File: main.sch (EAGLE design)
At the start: 100 parts, among them Q1 5.8A/30V/35mΩ, Q2 5.8A/30V/35mΩ, Q3 2.5A/30V/105mΩ, U2 SN65HVD32_D_8

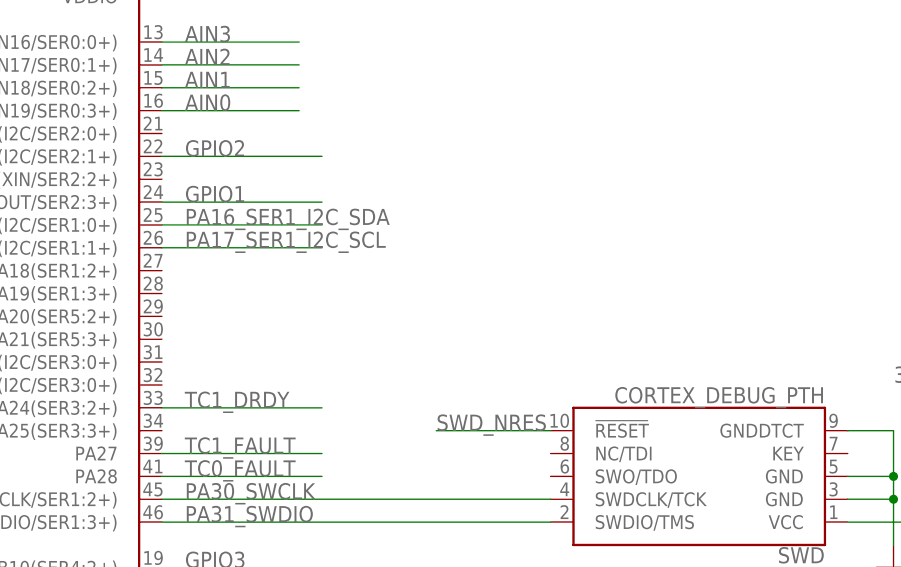
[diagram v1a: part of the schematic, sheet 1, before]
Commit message: Updated 3.3reg values, fixed led resitor, added one led to mcu
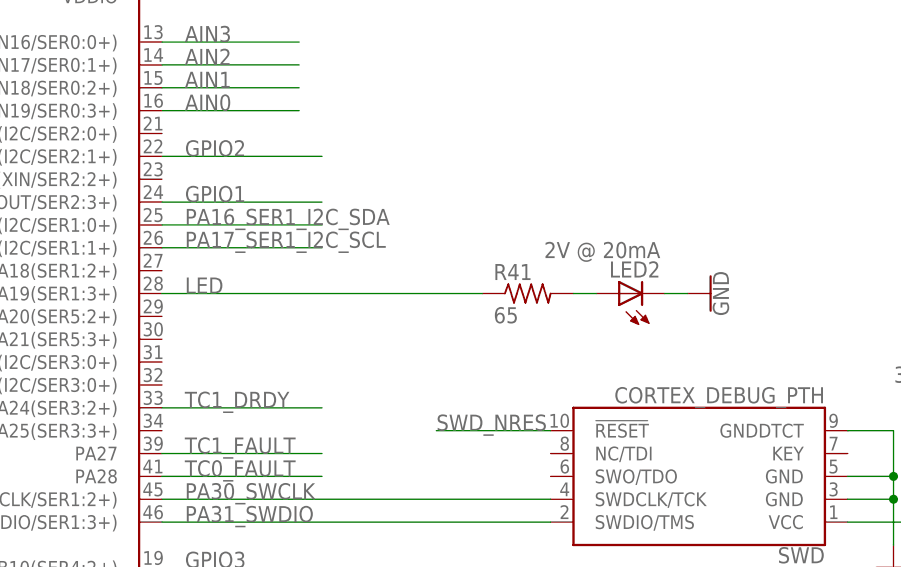
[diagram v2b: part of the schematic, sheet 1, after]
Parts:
- added LED2: 2V @ 20mA, adafruit:LEDCHIPLED_0603
- added R41: 65, resistor:R-US_R0603
- C6: value REF -> 22u
- C7: value REF -> 10u
- L1: value REF -> 2.2u
- LED1: value (none) -> 2V @ 20mA
- R1: value REF -> 470k
- R2: value REF -> 150k
- R3: value REF -> 100k
- R32: value 1.5k -> 65
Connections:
- new net LED: R41.1, SAMD21G18A.PA19(SER1:3+)
- new net N$29: LED2.A, R41.2
- net GND: now also LED2.C
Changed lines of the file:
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@@
 <part name="GND6" library="SparkFun-PowerSymbols" deviceset="GND" device=""/>
 <part name="GND7" library="SparkFun-PowerSymbols" deviceset="GND" device=""/>
-<part name="R1" library="resistor" library_urn="urn:adsk.eagle:library:348" deviceset="R-US_" device="R0603" package3d_urn="urn:adsk.eagle:package:26057/1" value="REF"/>
-<part name="R2" library="resistor" library_urn="urn:adsk.eagle:library:348" deviceset="R-US_" device="R0603" package3d_urn="urn:adsk.eagle:package:26057/1" value="REF"/>
-<part name="R3" library="resistor" library_urn="urn:adsk.eagle:library:348" deviceset="R-US_" device="R0603" package3d_urn="urn:adsk.eagle:package:26057/1" value="REF"/>
-<part name="L1" library="resistor" library_urn="urn:adsk.eagle:library:348" deviceset="L-US" device="L2012C" package3d_urn="urn:adsk.eagle:package:25925/1" value="REF"/>
-<part name="C6" library="resistor" library_urn="urn:adsk.eagle:library:348" deviceset="C-US" device="C0603" package3d_urn="urn:adsk.eagle:package:26138/1" value="REF"/>
+<part name="R1" library="resistor" library_urn="urn:adsk.eagle:library:348" deviceset="R-US_" device="R0603" package3d_urn="urn:adsk.eagle:package:26057/1" value="470k"/>
+<part name="R2" library="resistor" library_urn="urn:adsk.eagle:library:348" deviceset="R-US_" device="R0603" package3d_urn="urn:adsk.eagle:package:26057/1" value="150k"/>
+<part name="R3" library="resistor" library_urn="urn:adsk.eagle:library:348" deviceset="R-US_" device="R0603" package3d_urn="urn:adsk.eagle:package:26057/1" value="100k"/>
+<part name="L1" library="resistor" library_urn="urn:adsk.eagle:library:348" deviceset="L-US" device="L2012C" package3d_urn="urn:adsk.eagle:package:25925/1" value="2.2u"/>
+<part name="C6" library="resistor" library_urn="urn:adsk.eagle:library:348" deviceset="C-US" device="C0603" package3d_urn="urn:adsk.eagle:package:26138/1" value="22u"/>
 <part name="GND8" library="SparkFun-PowerSymbols" deviceset="GND" device=""/>
 <part name="SUPPLY14" library="SparkFun-PowerSymbols" deviceset="3.3V" device=""/>
-<part name="C7" library="rcl" library_urn="urn:adsk.eagle:library:334" deviceset="C-US" device="C1206" package3d_urn="urn:adsk.eagle:package:23618/2" value="REF"/>
+<part name="C7" library="rcl" library_urn="urn:adsk.eagle:library:334" deviceset="C-US" device="C1206" package3d_urn="urn:adsk.eagle:package:23618/2" value="10u"/>
 <part name="POWER_CONTROLLER" library="BQ24133" deviceset="BQ24133_RGY_24" device=""/>
 <part name="SUPPLY3" library="SparkFun-PowerSymbols" deviceset="3.3V" device=""/>
@@
 <part name="R31" library="resistor" library_urn="urn:adsk.eagle:library:348" deviceset="R-US_" device="R0603" package3d_urn="urn:adsk.eagle:package:26057/1" value="30.1k"/>
 <part name="GND36" library="SparkFun-PowerSymbols" deviceset="GND" device=""/>
-<part name="R32" library="resistor" library_urn="urn:adsk.eagle:library:348" deviceset="R-US_" device="R0603" package3d_urn="urn:adsk.eagle:package:26057/1" value="1.5k"/>
-<part name="LED1" library="adafruit" deviceset="LED" device="CHIPLED_0603"/>
+<part name="R32" library="resistor" library_urn="urn:adsk.eagle:library:348" deviceset="R-US_" device="R0603" package3d_urn="urn:adsk.eagle:package:26057/1" value="65"/>
+<part name="LED1" library="adafruit" deviceset="LED" device="CHIPLED_0603" value="2V @ 20mA"/>
 <part name="R_THERM" library="pinhead" library_urn="urn:adsk.eagle:library:325" deviceset="PINHD-1X2" device="" package3d_urn="urn:adsk.eagle:package:22435/2" value="103AT"/>
 <part name="R34" library="resistor" library_urn="urn:adsk.eagle:library:348" deviceset="R-US_" device="R0603" package3d_urn="urn:adsk.eagle:package:26057/1" value="100k"/>
@@
 <part name="R40" library="resistor" library_urn="urn:adsk.eagle:library:348" deviceset="R-US_" device="R0603" package3d_urn="urn:adsk.eagle:package:26057/1" value="10k"/>
 <part name="SUPPLY19" library="SparkFun-PowerSymbols" deviceset="3.3V" device=""/>
+<part name="R41" library="resistor" library_urn="urn:adsk.eagle:library:348" deviceset="R-US_" device="R0603" package3d_urn="urn:adsk.eagle:package:26057/1" value="65"/>
+<part name="LED2" library="adafruit" deviceset="LED" device="CHIPLED_0603" value="2V @ 20mA"/>
+<part name="GND50" library="SparkFun-PowerSymbols" deviceset="GND" device=""/>
 </parts>
 <sheets>
@@
 <instance part="R40" gate="G$1" x="304.8" y="165.1" rot="R90"/>
 <instance part="SUPPLY19" gate="G$1" x="304.8" y="172.72"/>
+<instance part="R41" gate="G$1" x="243.84" y="96.52"/>
+<instance part="LED2" gate="G$1" x="254" y="96.52" rot="R90"/>
+<instance part="GND50" gate="1" x="264.16" y="96.52" rot="R90"/>
 </instances>
 <busses>
@@
 <wire x1="294.64" y1="152.4" x2="304.8" y2="152.4" width="0.1524" layer="91"/>
 </segment>
+<segment>
+<pinref part="GND50" gate="1" pin="GND"/>
+<pinref part="LED2" gate="G$1" pin="C"/>
+<wire x1="261.62" y1="96.52" x2="259.08" y2="96.52" width="0.1524" layer="91"/>
+</segment>
 </net>
 <net name="VDDCORE" class="0">
@@
 </segment>
 </net>
+<net name="LED" class="0">
+<segment>
+<pinref part="R41" gate="G$1" pin="1"/>
+<pinref part="SAMD21G18A" gate="G$1" pin="PA19(SER1:3+)"/>
+<wire x1="238.76" y1="96.52" x2="203.2" y2="96.52" width="0.1524" layer="91"/>
+<label x="205.74" y="96.52" size="1.778" layer="95"/>
+</segment>
+</net>
+<net name="N$29" class="0">
+<segment>
+<pinref part="R41" gate="G$1" pin="2"/>
+<wire x1="248.92" y1="96.52" x2="251.46" y2="96.52" width="0.1524" layer="91"/>
+<pinref part="LED2" gate="G$1" pin="A"/>
+</segment>
+</net>

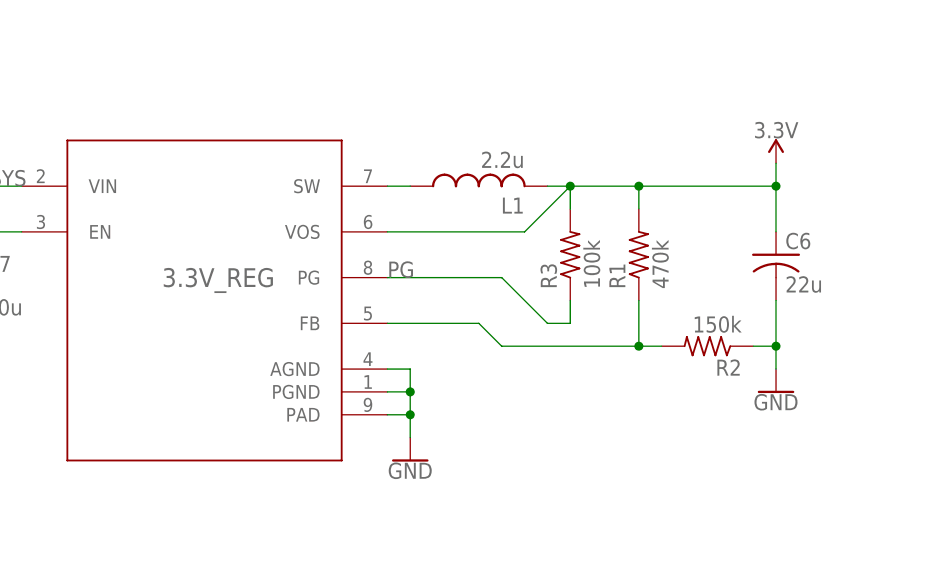
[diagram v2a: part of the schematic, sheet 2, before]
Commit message: Fixed 3.3v reg
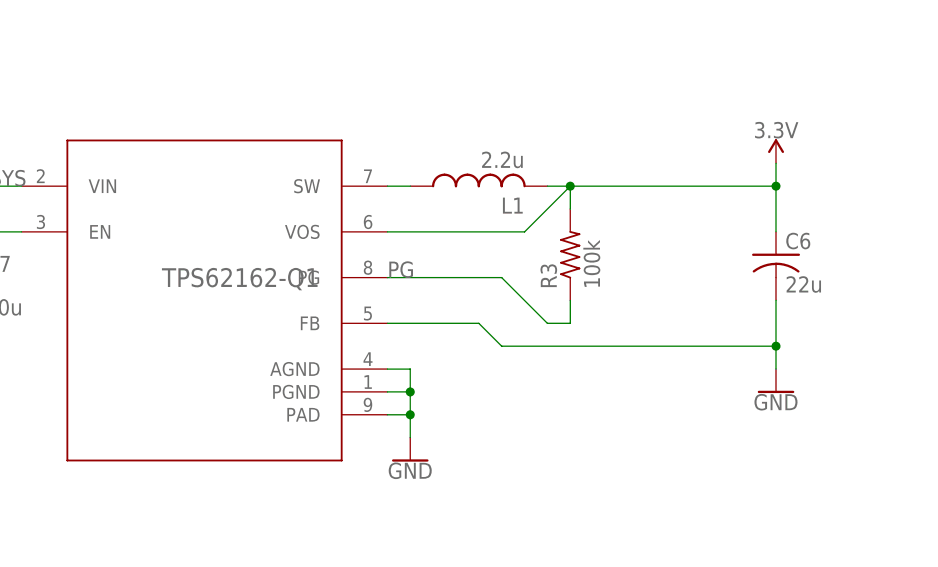
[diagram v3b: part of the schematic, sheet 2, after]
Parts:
- removed R1: 470k, resistor:R-US_R0603
- removed R2: 150k, resistor:R-US_R0603
- renumbered 3.3V_REG to TPS62162-Q1
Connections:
- removed net N$10: R1.1, R2.2, TPS62162-Q1.FB
- net 3.3V: no longer R1.2
- net GND: now also TPS62162-Q1.FB; no longer R2.1
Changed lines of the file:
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@@
 <?xml version="1.0" encoding="utf-8"?>
 <!DOCTYPE eagle SYSTEM "eagle.dtd">
-<eagle version="8.5.2">
+<eagle version="8.5.1">
 <drawing>
 <settings>
@@
 <part name="SUPPLY12" library="SparkFun-PowerSymbols" deviceset="3.3V" device=""/>
 <part name="IMU" library="BNO055" deviceset="BNO055" device=""/>
-<part name="3.3V_REG" library="TPS62162-Q1" deviceset="TPS62162QDSGRQ1" device="" value=""/>
+<part name="TPS62162-Q1" library="TPS62162-Q1" deviceset="TPS62162QDSGRQ1" device="" value=""/>
 <part name="GND6" library="SparkFun-PowerSymbols" deviceset="GND" device=""/>
 <part name="GND7" library="SparkFun-PowerSymbols" deviceset="GND" device=""/>
-<part name="R1" library="resistor" library_urn="urn:adsk.eagle:library:348" deviceset="R-US_" device="R0603" package3d_urn="urn:adsk.eagle:package:26057/1" value="470k"/>
-<part name="R2" library="resistor" library_urn="urn:adsk.eagle:library:348" deviceset="R-US_" device="R0603" package3d_urn="urn:adsk.eagle:package:26057/1" value="150k"/>
 <part name="R3" library="resistor" library_urn="urn:adsk.eagle:library:348" deviceset="R-US_" device="R0603" package3d_urn="urn:adsk.eagle:package:26057/1" value="100k"/>
 <part name="L1" library="resistor" library_urn="urn:adsk.eagle:library:348" deviceset="L-US" device="L2012C" package3d_urn="urn:adsk.eagle:package:25925/1" value="2.2u"/>
@@
 </plain>
 <instances>
-<instance part="3.3V_REG" gate="A" x="71.12" y="91.44"/>
+<instance part="TPS62162-Q1" gate="A" x="71.12" y="91.44"/>
 <instance part="GND6" gate="1" x="93.98" y="73.66"/>
 <instance part="GND7" gate="1" x="45.72" y="83.82"/>
-<instance part="R1" gate="G$1" x="119.38" y="96.52" rot="R90"/>
-<instance part="R2" gate="G$1" x="127" y="86.36" rot="R180"/>
 <instance part="R3" gate="G$1" x="111.76" y="96.52" rot="R90"/>
 <instance part="L1" gate="G$1" x="101.6" y="104.14" rot="R90"/>
@@
 <wire x1="109.22" y1="104.14" x2="111.76" y2="104.14" width="0.1524" layer="91"/>
 <wire x1="111.76" y1="104.14" x2="111.76" y2="101.6" width="0.1524" layer="91"/>
-<pinref part="3.3V_REG" gate="A" pin="VOS"/>
+<pinref part="TPS62162-Q1" gate="A" pin="VOS"/>
 <wire x1="91.44" y1="99.06" x2="106.68" y2="99.06" width="0.1524" layer="91"/>
 <wire x1="106.68" y1="99.06" x2="111.76" y2="104.14" width="0.1524" layer="91"/>
 <junction x="111.76" y="104.14"/>
-<wire x1="111.76" y1="104.14" x2="119.38" y2="104.14" width="0.1524" layer="91"/>
-<pinref part="R1" gate="G$1" pin="2"/>
-<wire x1="119.38" y1="104.14" x2="119.38" y2="101.6" width="0.1524" layer="91"/>
 <pinref part="R3" gate="G$1" pin="2"/>
 <pinref part="L1" gate="G$1" pin="2"/>
-<wire x1="119.38" y1="104.14" x2="134.62" y2="104.14" width="0.1524" layer="91"/>
-<junction x="119.38" y="104.14"/>
+<wire x1="111.76" y1="104.14" x2="134.62" y2="104.14" width="0.1524" layer="91"/>
 <pinref part="C6" gate="G$1" pin="1"/>
 <wire x1="134.62" y1="104.14" x2="134.62" y2="99.06" width="0.1524" layer="91"/>
@@
 <net name="GND" class="0">
 <segment>
-<pinref part="3.3V_REG" gate="A" pin="PGND"/>
+<pinref part="TPS62162-Q1" gate="A" pin="PGND"/>
 <wire x1="91.44" y1="81.28" x2="93.98" y2="81.28" width="0.1524" layer="91"/>
 <wire x1="93.98" y1="81.28" x2="93.98" y2="78.74" width="0.1524" layer="91"/>
@@
 <wire x1="93.98" y1="81.28" x2="93.98" y2="83.82" width="0.1524" layer="91"/>
 <junction x="93.98" y="81.28"/>
-<pinref part="3.3V_REG" gate="A" pin="AGND"/>
+<pinref part="TPS62162-Q1" gate="A" pin="AGND"/>
 <wire x1="93.98" y1="83.82" x2="91.44" y2="83.82" width="0.1524" layer="91"/>
 <pinref part="GND6" gate="1" pin="GND"/>
-<pinref part="3.3V_REG" gate="A" pin="PAD"/>
+<pinref part="TPS62162-Q1" gate="A" pin="PAD"/>
 <wire x1="91.44" y1="78.74" x2="93.98" y2="78.74" width="0.1524" layer="91"/>
 <junction x="93.98" y="78.74"/>
@@
 </segment>
 <segment>
-<pinref part="R2" gate="G$1" pin="1"/>
-<wire x1="132.08" y1="86.36" x2="134.62" y2="86.36" width="0.1524" layer="91"/>
 <pinref part="C6" gate="G$1" pin="2"/>
 <wire x1="134.62" y1="86.36" x2="134.62" y2="91.44" width="0.1524" layer="91"/>
@@
 <junction x="134.62" y="86.36"/>
 <pinref part="GND8" gate="1" pin="GND"/>
+<wire x1="134.62" y1="86.36" x2="104.14" y2="86.36" width="0.1524" layer="91"/>
+<pinref part="TPS62162-Q1" gate="A" pin="FB"/>
+<wire x1="91.44" y1="88.9" x2="101.6" y2="88.9" width="0.1524" layer="91"/>
+<wire x1="104.14" y1="86.36" x2="101.6" y2="88.9" width="0.1524" layer="91"/>
 </segment>
 <segment>
@@
 <net name="VSYS" class="0">
 <segment>
-<pinref part="3.3V_REG" gate="A" pin="VIN"/>
+<pinref part="TPS62162-Q1" gate="A" pin="VIN"/>
 <wire x1="50.8" y1="104.14" x2="45.72" y2="104.14" width="0.1524" layer="91"/>
-<pinref part="3.3V_REG" gate="A" pin="EN"/>
+<pinref part="TPS62162-Q1" gate="A" pin="EN"/>
 <wire x1="50.8" y1="99.06" x2="45.72" y2="99.06" width="0.1524" layer="91"/>
 <wire x1="45.72" y1="99.06" x2="45.72" y2="104.14" width="0.1524" layer="91"/>
@@
 <net name="N$7" class="0">
 <segment>
-<pinref part="3.3V_REG" gate="A" pin="SW"/>
+<pinref part="TPS62162-Q1" gate="A" pin="SW"/>
 <wire x1="93.98" y1="104.14" x2="91.44" y2="104.14" width="0.1524" layer="91"/>
 <pinref part="L1" gate="G$1" pin="1"/>
@@
 <net name="PG" class="0">
 <segment>
-<pinref part="3.3V_REG" gate="A" pin="PG"/>
+<pinref part="TPS62162-Q1" gate="A" pin="PG"/>
 <wire x1="91.44" y1="93.98" x2="104.14" y2="93.98" width="0.1524" layer="91"/>
 <wire x1="104.14" y1="93.98" x2="109.22" y2="88.9" width="0.1524" layer="91"/>
@@
 </segment>
 </net>
-<net name="N$10" class="0">
-<segment>
-<pinref part="R2" gate="G$1" pin="2"/>
-<pinref part="R1" gate="G$1" pin="1"/>
-<wire x1="119.38" y1="86.36" x2="121.92" y2="86.36" width="0.1524" layer="91"/>
-<wire x1="119.38" y1="91.44" x2="119.38" y2="86.36" width="0.1524" layer="91"/>
-<wire x1="119.38" y1="86.36" x2="104.14" y2="86.36" width="0.1524" layer="91"/>
-<junction x="119.38" y="86.36"/>
-<pinref part="3.3V_REG" gate="A" pin="FB"/>
-<wire x1="91.44" y1="88.9" x2="101.6" y2="88.9" width="0.1524" layer="91"/>
-<wire x1="104.14" y1="86.36" x2="101.6" y2="88.9" width="0.1524" layer="91"/>
-</segment>
-</net>

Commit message: Added new Battery Controller Model
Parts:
- added U1: BQ24133_RGY_24, BQ24133-UPDATED:BQ24133_RGY_24
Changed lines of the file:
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@@
 <?xml version="1.0" encoding="utf-8"?>
 <!DOCTYPE eagle SYSTEM "eagle.dtd">
-<eagle version="8.5.1">
+<eagle version="8.5.2">
 <drawing>
 <settings>
@@
 <part name="LED2" library="adafruit" deviceset="LED" device="CHIPLED_0603" value="2V @ 20mA"/>
 <part name="GND50" library="SparkFun-PowerSymbols" deviceset="GND" device=""/>
+<part name="U1" library="BQ24133-UPDATED" deviceset="BQ24133_RGY_24" device=""/>
 </parts>
 <sheets>
@@
 <instance part="GND40" gate="1" x="365.76" y="2.54"/>
 <instance part="S2" gate="1" x="464.82" y="114.3" rot="R90"/>
+<instance part="U1" gate="A" x="254" y="223.52"/>
 </instances>
 <busses>

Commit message: Removed Thermocouple ICs, Riped up everything, added a few more gpio pins
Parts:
- removed C10, C24, C27, C28, C29, C32: 100nF, resistor:C-USC0603
- removed C25, C26, C30, C31: 10nF, resistor:C-USC0603
- removed GPIO: (no value), pinhead:PINHD-1X3
- removed R22, R33, R36, R37: 100, resistor:R-US_R0603
- removed TC0, TC1: MAX31856, microbuilder:MAX31856
- removed TCIN0, TCIN1: (no value), pinhead:PINHD-1X2
- added JP1: (no value), pinhead:PINHD-1X5
- renumbered SAMD21G18A to MCU, SER4 to SD-CARD
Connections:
- removed net N$21: C10.1, C26.2, R33.2, TC0.T-
- removed net N$22: C10.2, C25.1, R22.2, TC0.T+
- removed net N$23: R33.1, TC0.BIAS, TCIN0.2
- removed net N$24: R22.1, TCIN0.1
- removed net N$25: C28.1, C31.2, R37.2, TC1.T-
- removed net N$26: C28.2, C30.1, R36.2, TC1.T+
- removed net N$27: R37.1, TC1.BIAS, TCIN1.2
- removed net N$28: R36.1, TCIN1.1
- removed net TC0_CS: MCU.PB02(AIN10/SER5:0), TC0.!CS
- removed net TC0_DRDY: MCU.PB03(AIN11/SER5:1), TC0.!DRDY
- removed net TC0_FAULT: MCU.PA28, TC0.!FAULT
- removed net TC1_CS: MCU.PA01(XOUT32/SER1:1/TC2:1), TC1.!CS
- removed net TC1_DRDY: MCU.PA24(SER3:2+), TC1.!DRDY
- removed net TC1_FAULT: MCU.PA27, TC1.!FAULT
- new net GPIO4: JP1.4
- new net GPIO5: JP1.5
- net 3.3V: no longer C24.1, C27.1, C29.1, C32.1, TC0.AVDD, TC0.DVDD, TC1.AVDD, TC1.DVDD
- net AIN0: no longer MCU.PA11(AIN19/SER0:3+)
- net AIN1: no longer MCU.PA10(AIN18/SER0:2+)
- net AIN2: no longer MCU.PA09(I2C/AIN17/SER0:1+)
- net AIN3: no longer MCU.PA08(I2C/AIN16/SER0:0+)
- net AIN4: no longer MCU.PA07(AIN7/SER0:3/TC1:1)
- net GND: no longer C24.2, C25.2, C26.1, C27.2, C29.2, C30.2, C31.1, C32.2, TC0.AGND, TC0.DGND, TC1.AGND, TC1.DGND
- net GPIO1: now also JP1.1; no longer GPIO.1, MCU.PA15(XOUT/SER2:3+)
- net GPIO2: now also JP1.2; no longer GPIO.2, MCU.PA13(I2C/SER2:1+)
- net GPIO3: now also JP1.3; no longer GPIO.3, MCU.PB10(SER4:2+)
- net PB08D_SER4_P0: no longer TC0.SDI, TC1.SDI
- net PB09D_SER4_P1: no longer TC0.SCK, TC1.SCK
- net PB11D_SER4_P3: no longer TC0.SDO, TC1.SDO
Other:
- moved on the sheet: BATT, C11, C12, C13, C14, C15, C16, C17, C18, C19, C20, C21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
